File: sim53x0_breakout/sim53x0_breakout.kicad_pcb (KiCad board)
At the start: 2 copper layers, 40 x 36 mm, 25 parts, among them J1 CONN_01X05, J4 CONN_01X06, J5 CONN_COAXIAL, J6 Conn_01x06, J7 Conn_01x07, J8 CONN_COAXIAL, J9 CONN_COAXIAL, U1 SIM5320

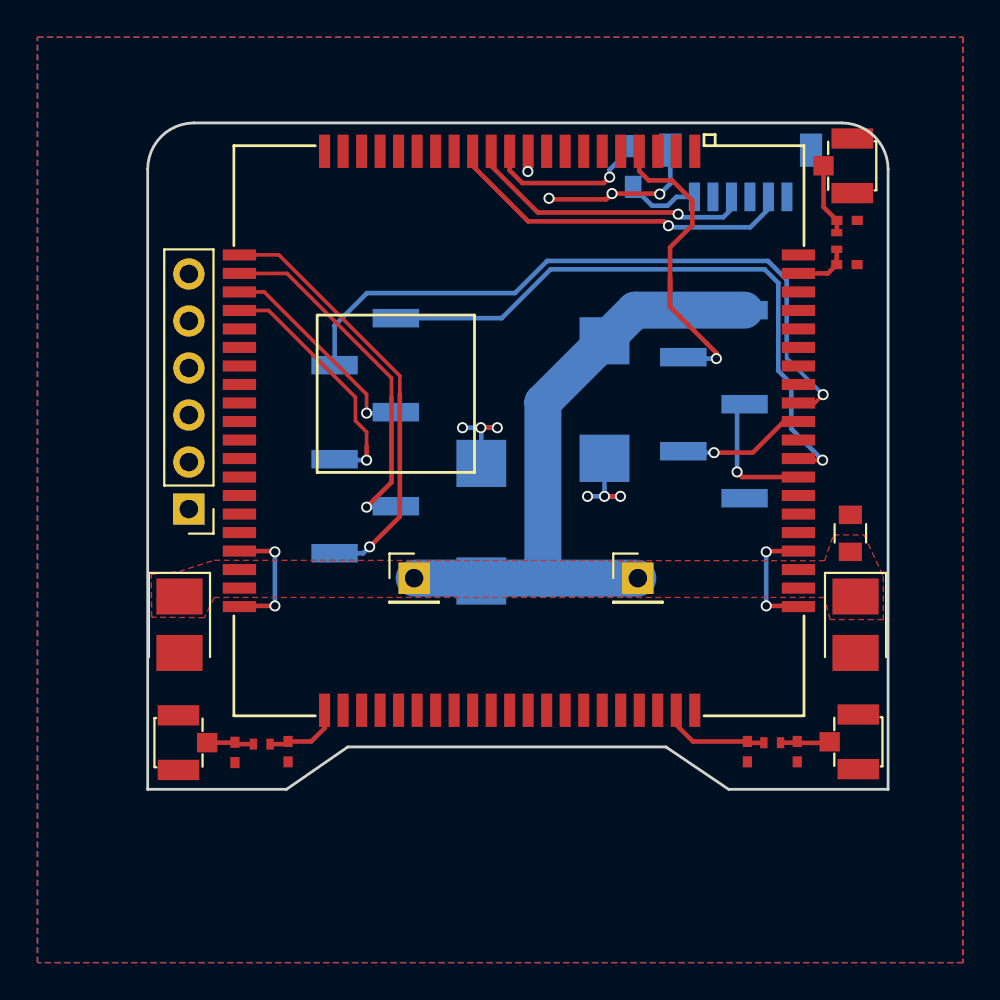
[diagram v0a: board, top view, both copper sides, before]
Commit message: Finished board - has limited usability! 3G modem too big
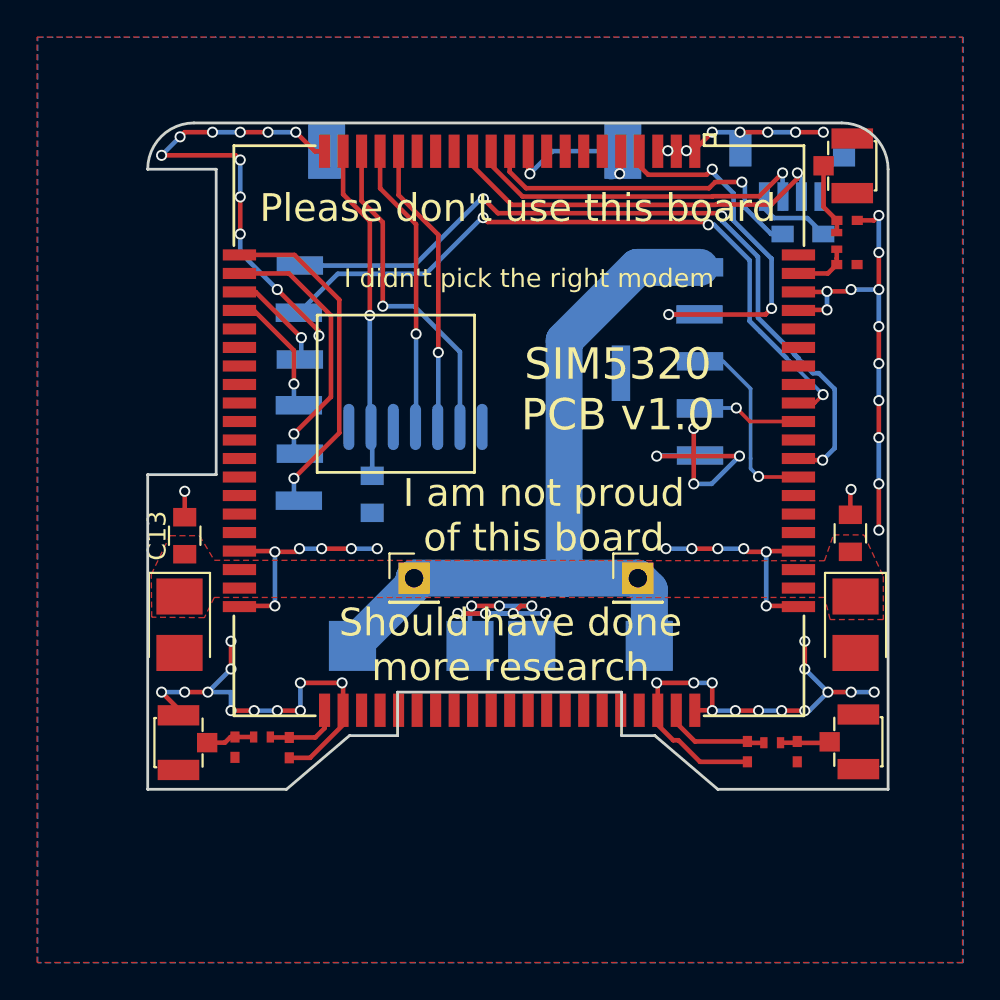
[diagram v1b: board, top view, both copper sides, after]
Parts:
- removed J6: Conn_01x06, Pin_Headers:Pin_Header_Straight_1x06_Pitch2.54mm
- removed J7: Conn_01x07, Connectors_JST:JST_SH_BM06B-SRSS-TB_06x1.00mm_Straight
- added ?: , footprints:Modem-Board-Outline, F.Cu at (26.9, 36.7)
- added C13: 100nF, Capacitors_SMD:C_0805, F.Cu at (122.0, 97.3)
- added C6: 100nF, Capacitors_SMD:C_0805, B.Cu at (132.1, 95.1)
- added J2: SIM_Card_with_Det, footprints:MICROSIM_6P_SMD_HOLDER, B.Cu at (137.7, 84.0)
- added J3: Conn_01x05, Connectors_JST:JST_SH_BM04B-SRSS-TB_04x1.00mm_Straight, B.Cu at (154.8, 77.7)
- J1: footprint Pin_Headers:Pin_Header_Straight_1x05_Pitch2.54mm_SMD_Pin1Left -> footprints:Pin_Header_Straight_1x05_Pitch2.54mm_SMD
- J4: footprint Pin_Headers:Pin_Header_Straight_1x06_Pitch2.54mm_SMD_Pin1Left -> footprints:Pin_Header_Straight_1x06_Pitch2.54mm_SMD
- moved C5 13.3 mm to (143.9, 103.2), turned to 180 degrees
- moved R1 9.87 mm to (155.4, 81.0), turned to 0 degrees
- moved C3 7.68 mm to (134.2, 103.3), turned to 0 degrees
- moved J4 5.92 mm to (126.6, 89.1)
- moved J1 3.34 mm to (148.2, 87.9)
- moved R5 0.38 mm to (126.2, 108.2)
- moved C9 0.28 mm to (124.7, 108.7)
- moved C7 0.23 mm to (127.7, 108.8)
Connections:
- U1 pad 17: (no net) -> Net-(J2-Pad5)
- U1 pad 18: (no net) -> Net-(J2-Pad4)
- U1 pad 19: (no net) -> Net-(J2-Pad6)
- U1 pad 20: (no net) -> Net-(C6-Pad1)
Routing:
- net GND: track 32.5 -> 173.8 mm, vias 14 -> 81
- net Net-(C6-Pad1): track 0.00 -> 18.2 mm, vias 0 -> 1
- net Net-(J2-Pad6): track 0.00 -> 18.1 mm, vias 0 -> 1
- net Net-(J2-Pad5): track 0.00 -> 15.8 mm, vias 0 -> 1
- net Net-(J2-Pad4): track 0.00 -> 15.7 mm, vias 0 -> 1
- net Net-(R1-Pad1): track 9.05 -> 18.2 mm
- net RING: track 34.0 -> 42.5 mm, vias 1 -> 3
- net VDD: track 38.3 -> 46.6 mm
- net MIC-: track 13.6 -> 6.91 mm
- net MIC+: track 11.8 -> 5.58 mm
- net SPK+: track 19.7 -> 14.3 mm
- net SPK-: track 23.3 -> 18.4 mm
- net RESET: track 17.2 -> 22.0 mm, vias 1 -> 3
- net /D-: track 15.8 -> 19.7 mm
- net RXD: track 7.36 -> 10.4 mm
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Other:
- outline, holes or cut-outs redrawn
- board text added: "I am not proud of this board"
- board text added: "I didn't pick the right modem"
- board text added: "Please don't use this board"
- board text added: "SIM5320 PCB v1.0"
- board text added: "Should have done more research"

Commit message: Small silkscreen adjustments
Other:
- board text added: "SIM5320 PCB v-last"
- board text added: "SIM5320 PCB v... last version"
- board text removed: "SIM5320 PCB v1.0"
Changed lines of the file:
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@@
     (area 119.924999 74.924999 160.075001 111.075001)
     (thickness 1.6)
-    (drawings 22)
+    (drawings 23)
     (tracks 418)
     (zones 0)
@@
   (module footprints:MICROSIM_6P_SMD_HOLDER (layer B.Cu)
     (at 137.668 84.0232 180)
-    (fp_text reference J2 (at -5.2 -9.2 180) (layer B.SilkS)
+    (fp_text reference J2 (at -5.2 -9.2 180) (layer B.SilkS) hide
       (effects (font (size 1 1) (thickness 0.15)) (justify mirror))
     )
@@
     (tags "capacitor 0805")
     (attr smd)
-    (fp_text reference C13 (at 0 -1.5 90) (layer F.SilkS)
+    (fp_text reference C13 (at 0 -1.5 90) (layer F.SilkS) hide
       (effects (font (size 1 1) (thickness 0.15)))
     )
@@
     )
   )
+  (gr_text "SIM5320\nPCB v-last" (at 145.5 89.5) (layer F.SilkS)
+    (effects (font (size 1.7 1.7) (thickness 0.3)))
+  )
   (gr_text "Please don't use this board" (at 140 79.6) (layer F.SilkS)
     (effects (font (size 1.5 1.5) (thickness 0.3)))
@@
     (effects (font (size 1.5 1.5) (thickness 0.3)))
   )
-  (gr_text "SIM5320\nPCB v1.0" (at 145.4 89.4) (layer F.SilkS)
-    (effects (font (size 1.7 1.7) (thickness 0.3)))
+  (gr_text "SIM5320\nPCB v... last version" (at 141 96) (layer B.SilkS)
+    (effects (font (size 1.7 1.7) (thickness 0.3)) (justify mirror))
   )
   (gr_line (start 133.5 108.1) (end 130.9 108.1) (layer Edge.Cuts) (width 0.15))
